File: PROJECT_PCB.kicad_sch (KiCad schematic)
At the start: 25 parts, among them J1 SS-52400-003, J2 B2B-PH-K-S_LF__SN_, U1 MCP73871

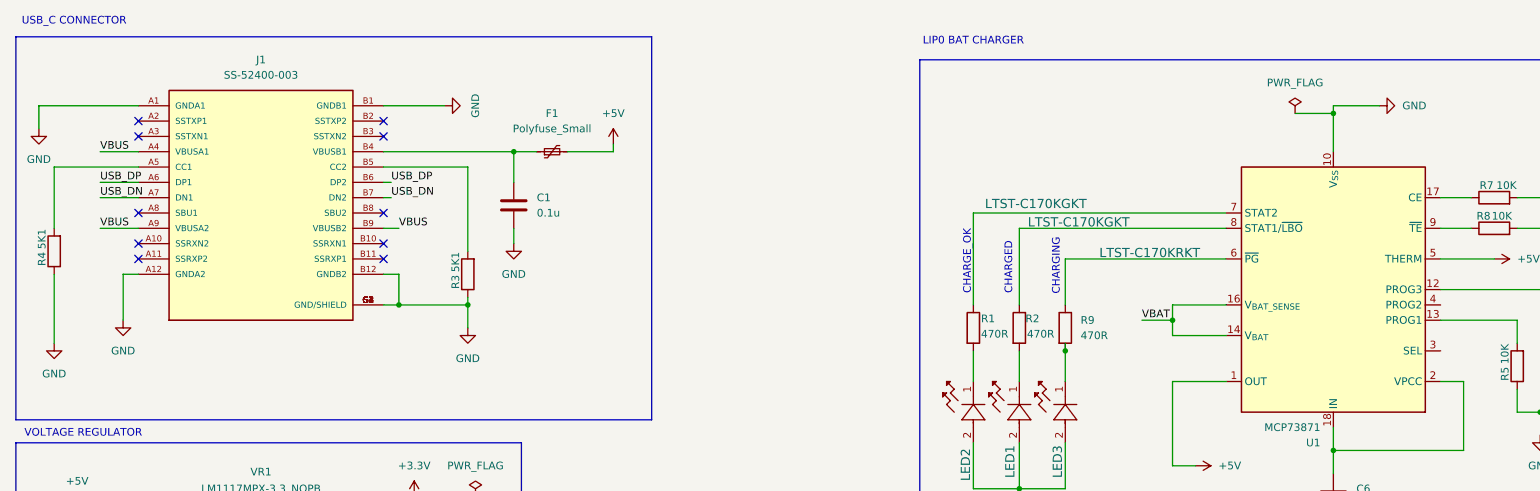
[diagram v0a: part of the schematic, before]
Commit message: update added esp32,uart , sd card and flash memory schematic
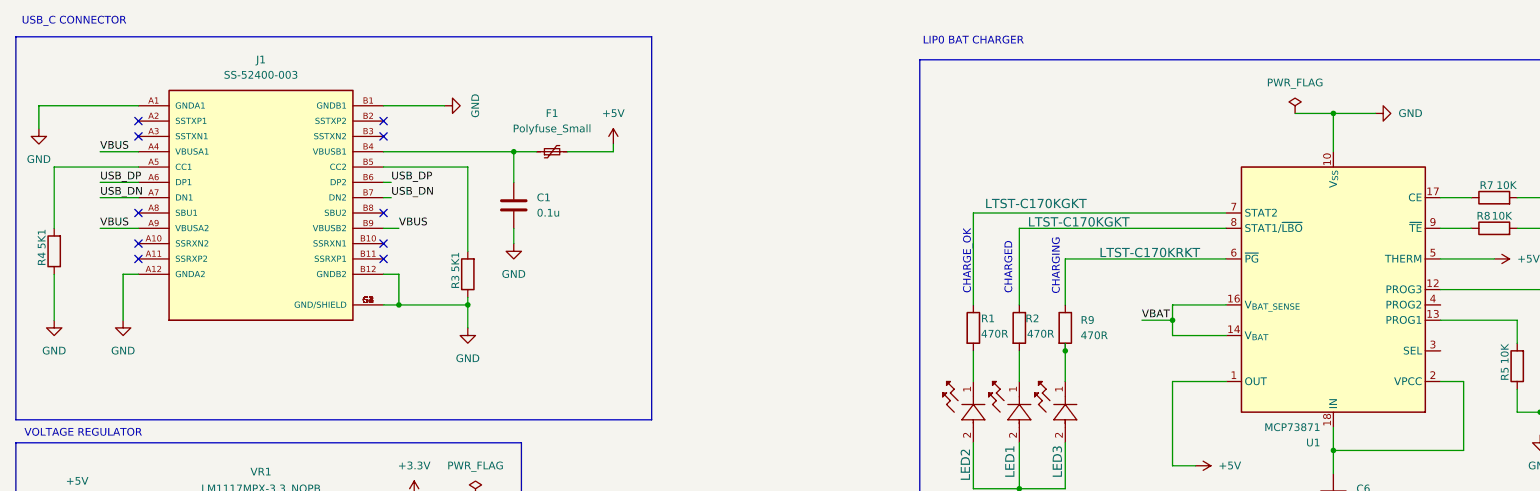
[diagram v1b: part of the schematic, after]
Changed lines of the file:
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@@
 	(wire
 		(pts
-			(xy 231.14 31.75) (xy 231.14 30.48)
-		)
-		(stroke
-			(width 0)
-			(type default)
-		)
-	)
-	(wire
-		(pts
 			(xy 27.94 113.03) (xy 27.94 116.84)
 		)
@@
 	(wire
 		(pts
-			(xy 231.14 30.48) (xy 238.76 30.48)
+			(xy 231.14 31.75) (xy 238.125 31.75)
 		)
 		(stroke
@@
 	(wire
 		(pts
-			(xy 19.05 58.42) (xy 19.05 69.85)
+			(xy 19.05 58.42) (xy 19.05 66.04)
 		)
 		(stroke
@@
 	(symbol
 		(lib_id "power:GND")
-		(at 238.76 30.48 90)
+		(at 238.125 31.75 90)
 		(unit 1)
 		(exclude_from_sim no)
@@
 		(fields_autoplaced yes)
 		(property "Reference" "#PWR09"
-			(at 245.11 30.48 0)
+			(at 244.475 31.75 0)
 			(effects
 				(font
@@
 		)
 		(property "Value" "GND"
-			(at 242.57 30.4799 90)
+			(at 241.935 31.7499 90)
 			(effects
 				(font
@@
 		)
 		(property "Footprint" ""
-			(at 238.76 30.48 0)
+			(at 238.125 31.75 0)
 			(effects
 				(font
@@
 		)
 		(property "Datasheet" ""
-			(at 238.76 30.48 0)
+			(at 238.125 31.75 0)
 			(effects
 				(font
@@
 		)
 		(property "Description" "Power symbol creates a global label with name \"GND\" , ground"
-			(at 238.76 30.48 0)
+			(at 238.125 31.75 0)
 			(effects
 				(font
@@
 	(symbol
 		(lib_id "power:GND")
-		(at 19.05 69.85 0)
+		(at 19.05 66.04 0)
 		(unit 1)
 		(exclude_from_sim no)
@@
 		(fields_autoplaced yes)
 		(property "Reference" "#PWR04"
-			(at 19.05 76.2 0)
+			(at 19.05 72.39 0)
 			(effects
 				(font
@@
 		)
 		(property "Value" "GND"
-			(at 19.05 74.93 0)
+			(at 19.05 71.12 0)
 			(effects
 				(font
@@
 		)
 		(property "Footprint" ""
-			(at 19.05 69.85 0)
+			(at 19.05 66.04 0)
 			(effects
 				(font
@@
 		)
 		(property "Datasheet" ""
-			(at 19.05 69.85 0)
+			(at 19.05 66.04 0)
 			(effects
 				(font
@@
 		)
 		(property "Description" "Power symbol creates a global label with name \"GND\" , ground"
-			(at 19.05 69.85 0)
+			(at 19.05 66.04 0)
 			(effects
 				(font

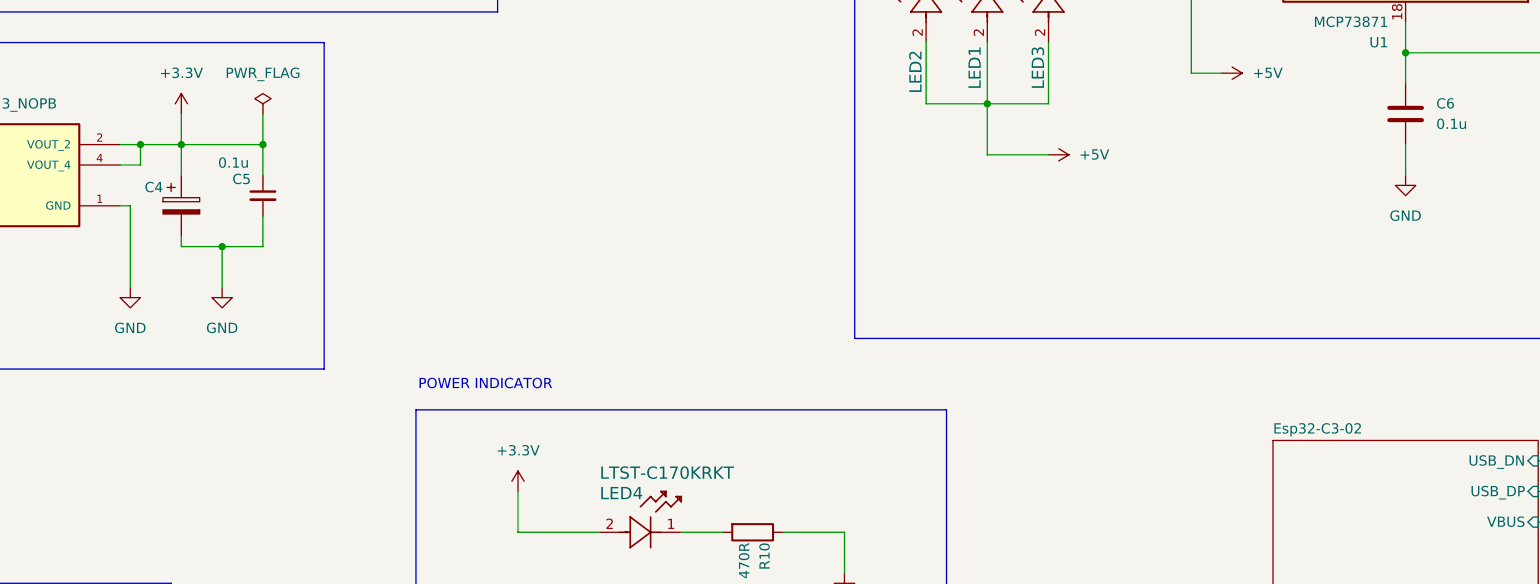
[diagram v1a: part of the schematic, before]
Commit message: update the main file schematic
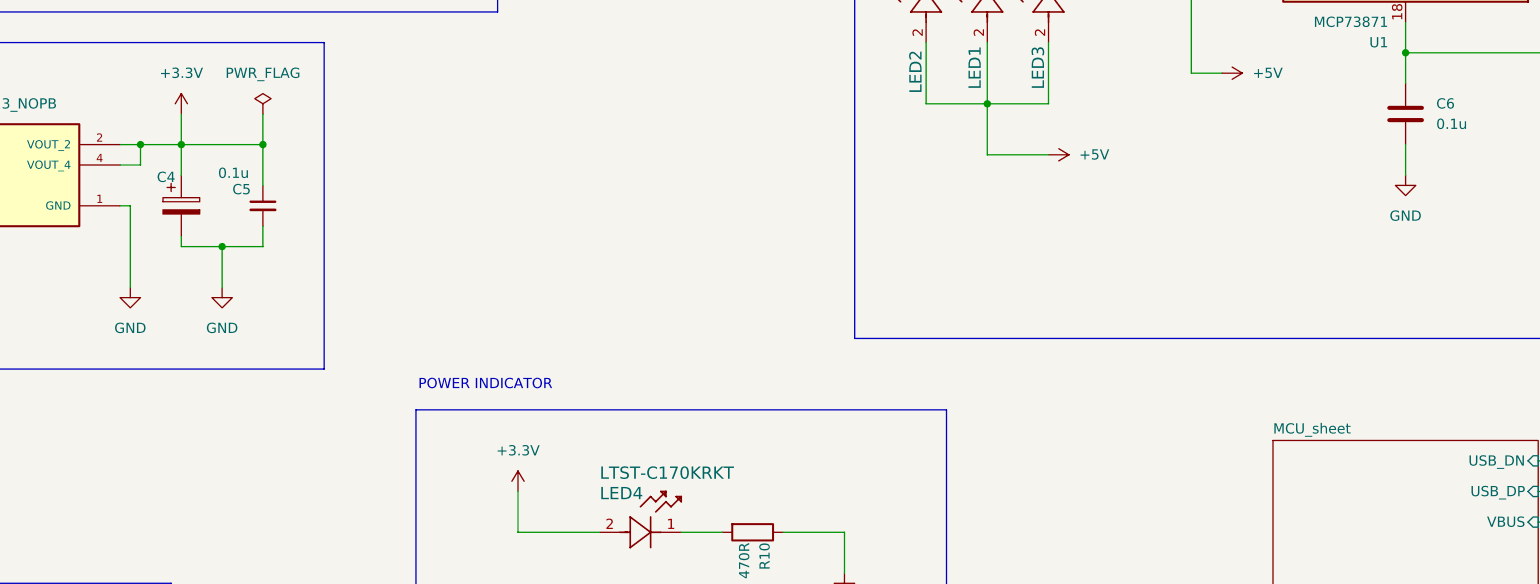
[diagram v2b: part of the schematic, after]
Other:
- sheet Esp32-C3-02 renamed MCU_sheet
- moved on the sheet: C5
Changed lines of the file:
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@@
 	(wire
 		(pts
-			(xy 88.9 107.95) (xy 88.9 111.76)
+			(xy 88.9 109.22) (xy 88.9 111.76)
 		)
 		(stroke
@@
 	(wire
 		(pts
-			(xy 88.9 102.87) (xy 88.9 99.06)
+			(xy 88.9 104.14) (xy 88.9 99.06)
 		)
 		(stroke
@@
 	(symbol
 		(lib_id "Device:C_Small")
-		(at 88.9 105.41 0)
+		(at 88.9 106.68 0)
 		(unit 1)
 		(exclude_from_sim no)
@@
 		(dnp no)
 		(property "Reference" "C5"
-			(at 85.09 103.378 0)
+			(at 85.09 104.648 0)
 			(effects
 				(font
@@
 		)
 		(property "Value" "0.1u"
-			(at 83.312 101.346 0)
+			(at 83.312 102.616 0)
 			(effects
 				(font
@@
 		)
 		(property "Footprint" ""
-			(at 88.9 105.41 0)
+			(at 88.9 106.68 0)
 			(effects
 				(font
@@
 		)
 		(property "Datasheet" "~"
-			(at 88.9 105.41 0)
+			(at 88.9 106.68 0)
 			(effects
 				(font
@@
 		)
 		(property "Description" "Unpolarized capacitor, small symbol"
-			(at 88.9 105.41 0)
+			(at 88.9 106.68 0)
 			(effects
 				(font
@@
 		(dnp no)
 		(property "Reference" "C4"
-			(at 74.168 104.394 0)
+			(at 75.692 103.124 0)
 			(effects
 				(font
@@
 			(color 0 0 0 0.0000)
 		)
-		(property "Sheetname" "Esp32-C3-02"
+		(property "Sheetname" "MCU_sheet"
 			(at 214.63 135.1784 0)
 			(effects

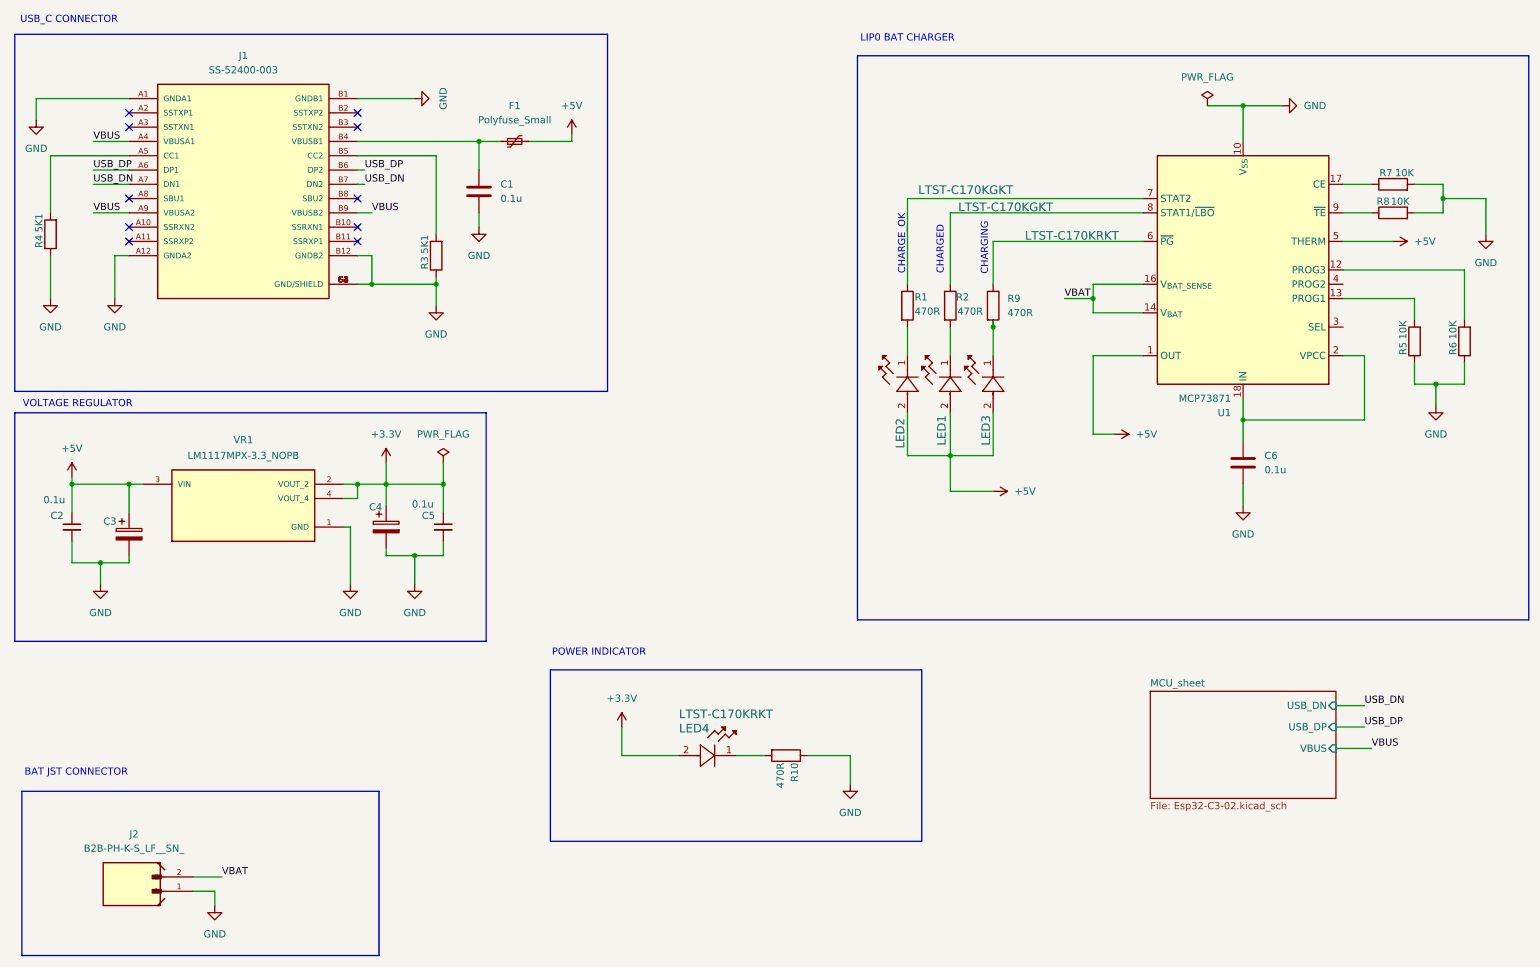
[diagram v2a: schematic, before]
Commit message: run ERC check for the schematic
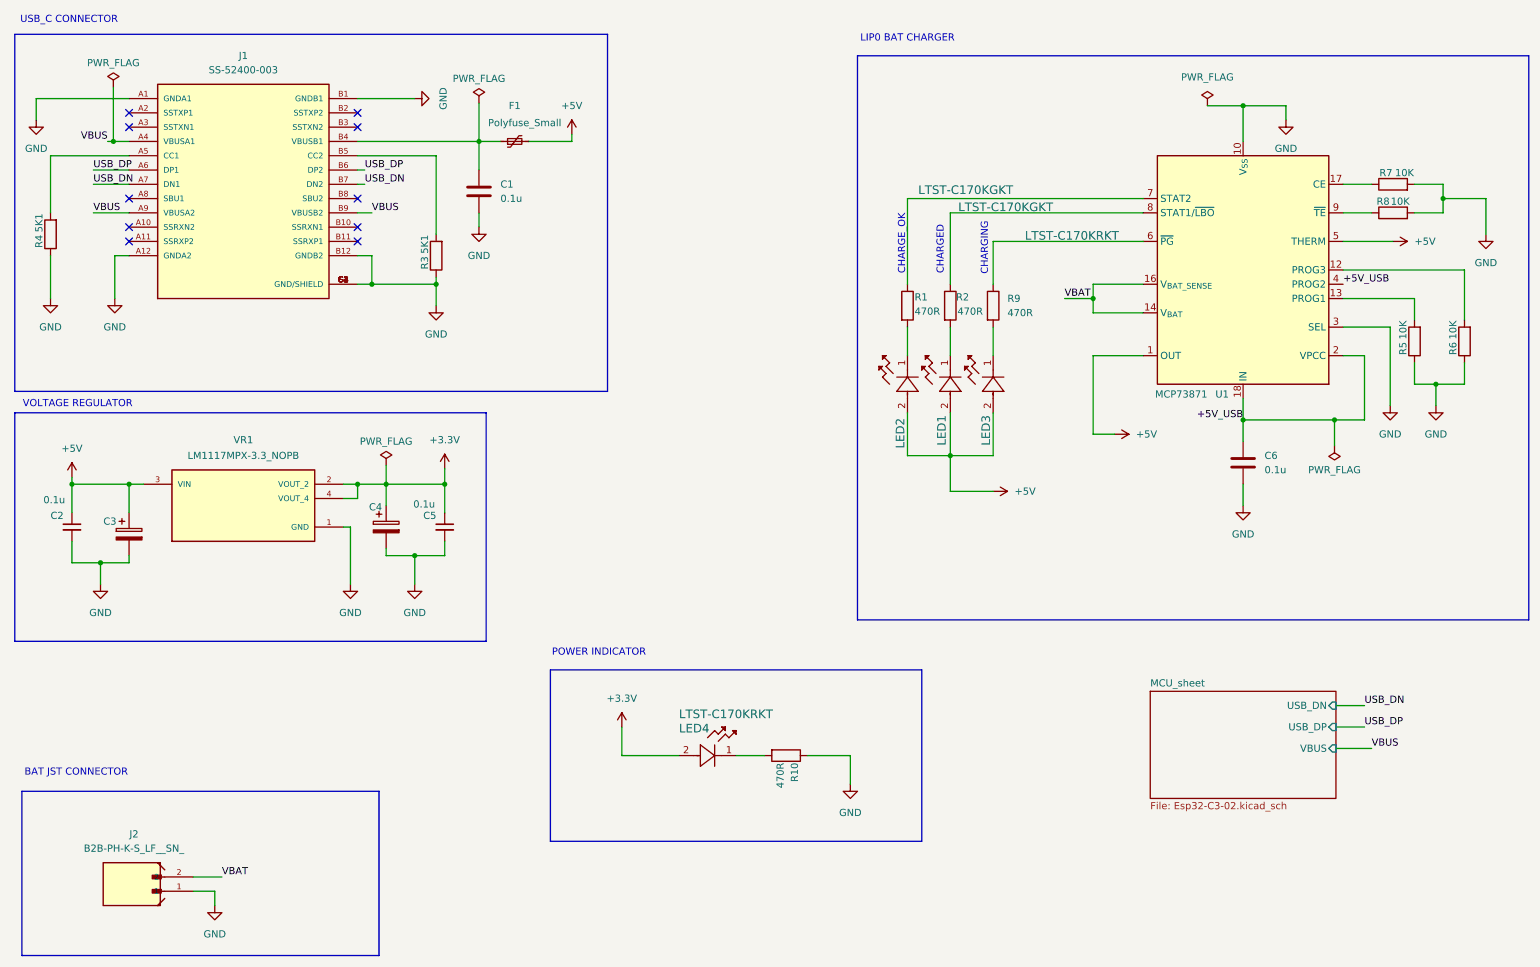
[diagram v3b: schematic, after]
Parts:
- C1, C2, C5, C6: footprint (none) -> Capacitor_SMD:C_0805_2012Metric
- C3, C4: footprint (none) -> Capacitor_Tantalum_SMD:CP_EIA-7343-40_Kemet-Y
- F1: footprint (none) -> Fuse:Fuse_BelFuse_0ZRE0016FF_L9.9mm_W3.8mm
- LED1, LED2: footprint LED_LTST-C170KGKT_LTO -> LED_SMD:LED_0805_2012Metric
- LED3, LED4: footprint LED_LTST-C170KRKT_LTO -> LED_SMD:LED_0805_2012Metric
- R1, R10, R2, R3, R4, R5, R6, R7, R8, R9: footprint (none) -> Resistor_SMD:R_0805_2012Metric
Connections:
- net GND: now also U1.3 (SEL)
- net +5V_USB: now reaches C6.1, U1.18 (IN), U1.19 (IN), U1.2 (VPCC)
- net +5V_USB: now also U1.4 (PROG2)

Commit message: assigning footprint, pcb setup and configurations
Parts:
- C3, C4: footprint Capacitor_Tantalum_SMD:CP_EIA-7343-40_Kemet-Y -> FootPrints:CAPMP3216X180N
- J1: footprint Connector_USB:BELFUSE_SS-52400-003 -> SS-52400-003:BELFUSE_SS-52400-003
- J2: footprint B2B-PH-K-S_LF__SN_:JST_B2B-PH-K-S_LF__SN_ -> FootPrints:JST_B2B-PH-K-S_LF__SN_
- VR1: footprint LM1117MPX-3.3_NOPB:VREG_LM1117MPX-3.3_NOPB -> FootPrints:VREG_LM1117MPX-3.3_NOPB
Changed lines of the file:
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@@
 			)
 		)
-		(property "Footprint" "Connector_USB:BELFUSE_SS-52400-003"
+		(property "Footprint" "SS-52400-003:BELFUSE_SS-52400-003"
 			(at 53.34 45.72 0)
 			(effects
@@
 			)
 		)
-		(property "Footprint" "B2B-PH-K-S_LF__SN_:JST_B2B-PH-K-S_LF__SN_"
+		(property "Footprint" "FootPrints:JST_B2B-PH-K-S_LF__SN_"
 			(at 34.29 168.91 0)
 			(effects
@@
 			)
 		)
-		(property "Footprint" "LM1117MPX-3.3_NOPB:VREG_LM1117MPX-3.3_NOPB"
+		(property "Footprint" "FootPrints:VREG_LM1117MPX-3.3_NOPB"
 			(at 53.34 101.6 0)
 			(effects
@@
 			)
 		)
-		(property "Footprint" "Capacitor_Tantalum_SMD:CP_EIA-7343-40_Kemet-Y"
+		(property "Footprint" "FootPrints:CAPMP3216X180N"
 			(at 33.9852 111.76 0)
 			(effects
@@
 			)
 		)
-		(property "Footprint" "Capacitor_Tantalum_SMD:CP_EIA-7343-40_Kemet-Y"
+		(property "Footprint" "FootPrints:CAPMP3216X180N"
 			(at 79.7052 110.49 0)
 			(effects

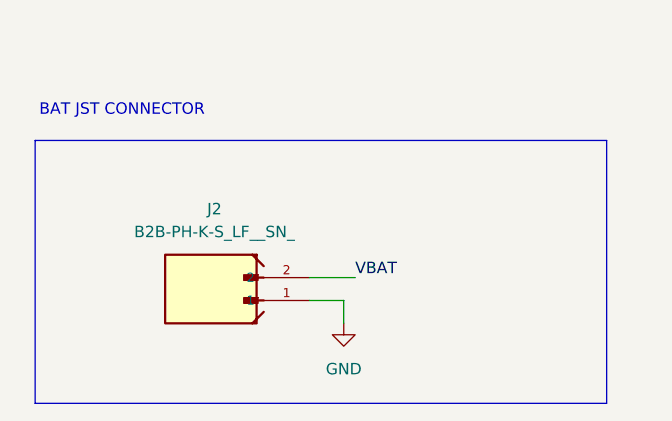
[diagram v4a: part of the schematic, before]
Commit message: PCB outlining and component placement
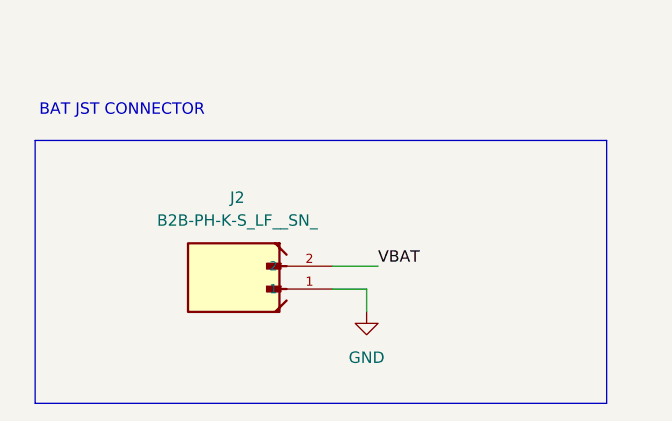
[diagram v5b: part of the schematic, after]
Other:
- moved on the sheet: J2
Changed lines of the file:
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@@
 	(wire
 		(pts
-			(xy 48.26 171.45) (xy 48.26 173.99)
+			(xy 50.8 170.18) (xy 50.8 172.72)
 		)
 		(stroke
@@
 	(wire
 		(pts
-			(xy 44.45 171.45) (xy 48.26 171.45)
+			(xy 46.99 170.18) (xy 50.8 170.18)
 		)
 		(stroke
@@
 	(wire
 		(pts
-			(xy 44.45 168.91) (xy 49.53 168.91)
+			(xy 46.99 167.64) (xy 52.07 167.64)
 		)
 		(stroke
@@
 	)
 	(label "VBAT"
-		(at 49.53 168.91 0)
+		(at 52.07 167.64 0)
 		(effects
 			(font
@@
 	(symbol
 		(lib_id "B2B-PH-K-S_LF__SN_:B2B-PH-K-S_LF__SN_")
-		(at 34.29 168.91 180)
+		(at 36.83 167.64 180)
 		(unit 1)
 		(exclude_from_sim no)
@@
 		(fields_autoplaced yes)
 		(property "Reference" "J2"
-			(at 33.8931 161.29 0)
+			(at 36.4331 160.02 0)
 			(effects
 				(font
@@
 		)
 		(property "Value" "B2B-PH-K-S_LF__SN_"
-			(at 33.8931 163.83 0)
+			(at 36.4331 162.56 0)
 			(effects
 				(font
@@
 		)
 		(property "Footprint" "FootPrints:JST_B2B-PH-K-S_LF__SN_"
-			(at 34.29 168.91 0)
+			(at 36.83 167.64 0)
 			(effects
 				(font
@@
 		)
 		(property "Datasheet" ""
-			(at 34.29 168.91 0)
+			(at 36.83 167.64 0)
 			(effects
 				(font
@@
 		)
 		(property "Description" ""
-			(at 34.29 168.91 0)
+			(at 36.83 167.64 0)
 			(effects
 				(font
@@
 		)
 		(property "MF" "JST"
-			(at 34.29 168.91 0)
+			(at 36.83 167.64 0)
 			(effects
 				(font
@@
 		)
 		(property "Description_1" "2.0 mm pitch/Disconnectable Crimp style connectors"
-			(at 34.29 168.91 0)
+			(at 36.83 167.64 0)
 			(effects
 				(font
@@
 		)
 		(property "Package" "None"
-			(at 34.29 168.91 0)
+			(at 36.83 167.64 0)
 			(effects
 				(font
@@
 		)
 		(property "Price" "None"
-			(at 34.29 168.91 0)
+			(at 36.83 167.64 0)
 			(effects
 				(font
@@
 		)
 		(property "Check_prices" "https://www.snapeda.com/parts/B2B-PH-K-S(LF)(SN)/JST/view-part/?ref=eda"
-			(at 34.29 168.91 0)
+			(at 36.83 167.64 0)
 			(effects
 				(font
@@
 		)
 		(property "SnapEDA_Link" "https://www.snapeda.com/parts/B2B-PH-K-S(LF)(SN)/JST/view-part/?ref=snap"
-			(at 34.29 168.91 0)
+			(at 36.83 167.64 0)
 			(effects
 				(font
@@
 		)
 		(property "MP" "B2B-PH-K-S(LF)(SN)"
-			(at 34.29 168.91 0)
+			(at 36.83 167.64 0)
 			(effects
 				(font
@@
 		)
 		(property "Availability" "In Stock"
-			(at 34.29 168.91 0)
+			(at 36.83 167.64 0)
 			(effects
 				(font
@@
 		)
 		(property "MANUFACTURER" "JST"
-			(at 34.29 168.91 0)
+			(at 36.83 167.64 0)
 			(effects
 				(font
@@
 	(symbol
 		(lib_id "power:GND")
-		(at 48.26 173.99 0)
+		(at 50.8 172.72 0)
 		(unit 1)
 		(exclude_from_sim no)
@@
 		(fields_autoplaced yes)
 		(property "Reference" "#PWR020"
-			(at 48.26 180.34 0)
+			(at 50.8 179.07 0)
 			(effects
 				(font
@@
 		)
 		(property "Value" "GND"
-			(at 48.26 179.07 0)
+			(at 50.8 177.8 0)
 			(effects
 				(font
@@
 		)
 		(property "Footprint" ""
-			(at 48.26 173.99 0)
+			(at 50.8 172.72 0)
 			(effects
 				(font
@@
 		)
 		(property "Datasheet" ""
-			(at 48.26 173.99 0)
+			(at 50.8 172.72 0)
 			(effects
 				(font
@@
 		)
 		(property "Description" "Power symbol creates a global label with name \"GND\" , ground"
-			(at 48.26 173.99 0)
+			(at 50.8 172.72 0)
 			(effects
 				(font
